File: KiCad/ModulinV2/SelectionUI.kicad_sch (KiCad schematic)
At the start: 24 parts, among them IC16 E-ULN2003D1013TR, IC17 E-ULN2003D1013TR, IC18 CD4028BM96, IC19 CD4028BM96

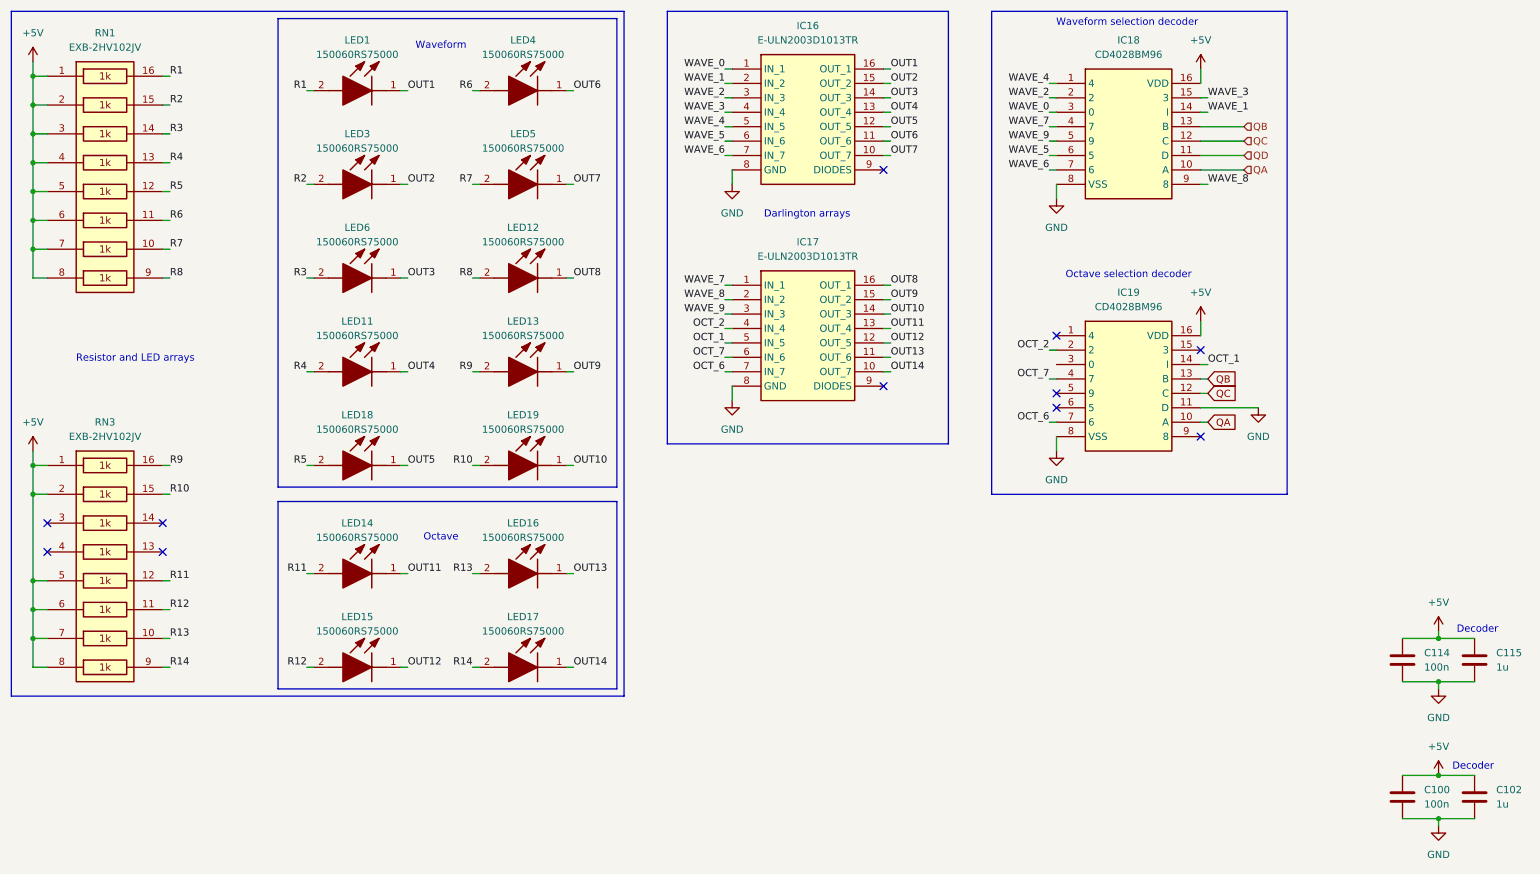
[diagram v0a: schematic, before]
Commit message: Changed switch for the boot and nrst. Fixed the GATE interface trigger
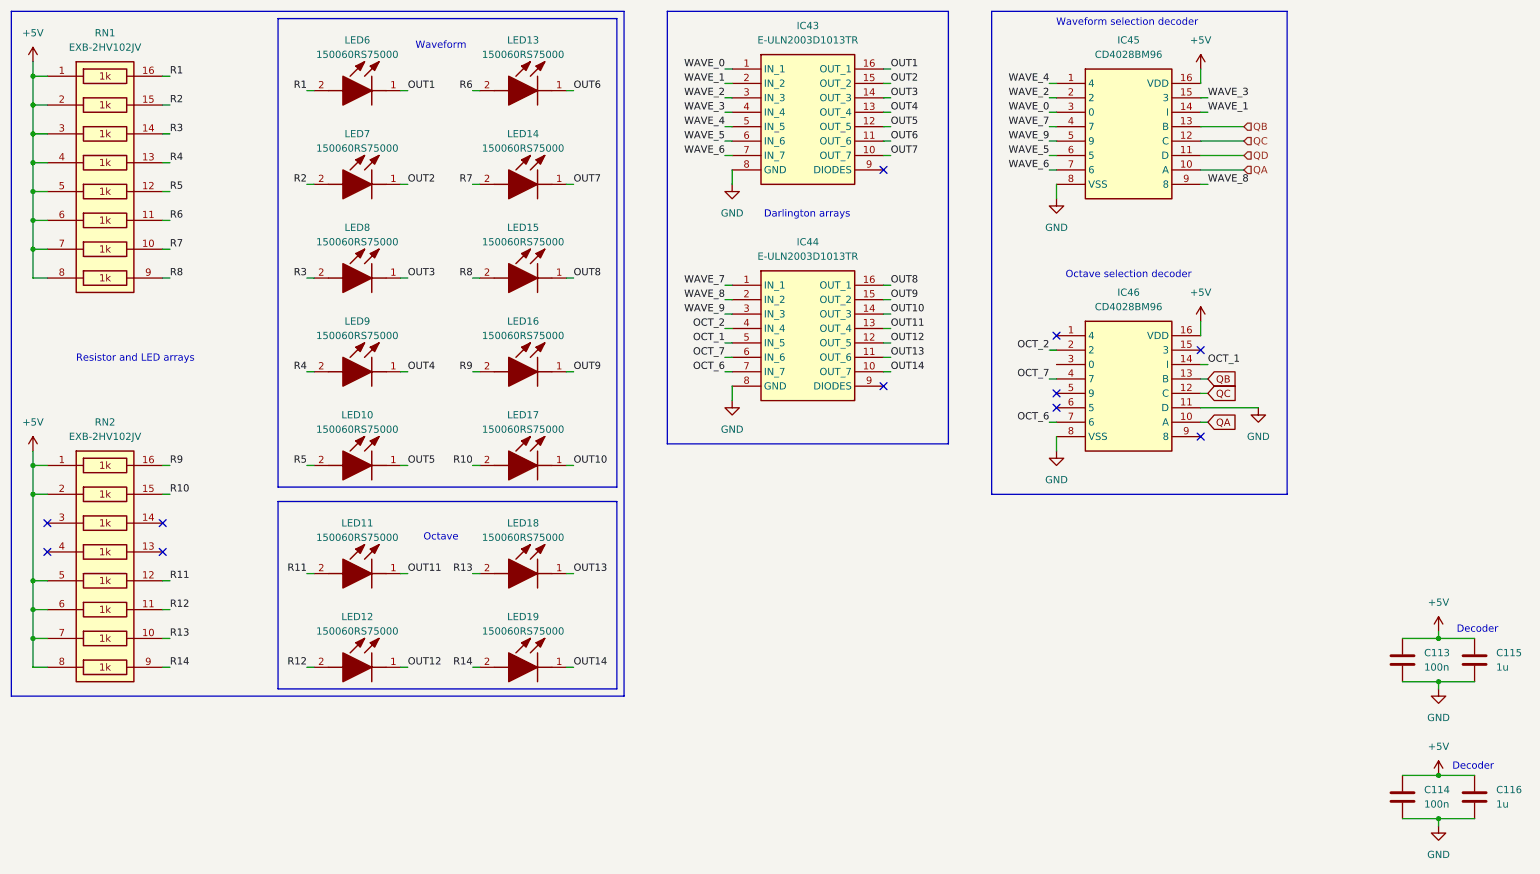
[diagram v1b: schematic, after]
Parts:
- renumbered C114 to C113, C100 to C114, C102 to C116, IC16 to IC43, IC17 to IC44, IC18 to IC45, IC19 to IC46, LED18 to LED10, LED14 to LED11, LED15 to LED12, LED4 to LED13, LED5 to LED14, LED12 to LED15, LED13 to LED16, LED19 to LED17, LED16 to LED18, LED17 to LED19, LED1 to LED6, LED3 to LED7, LED6 to LED8, LED11 to LED9, RN3 to RN2

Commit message: Started adding footprints for capacitors
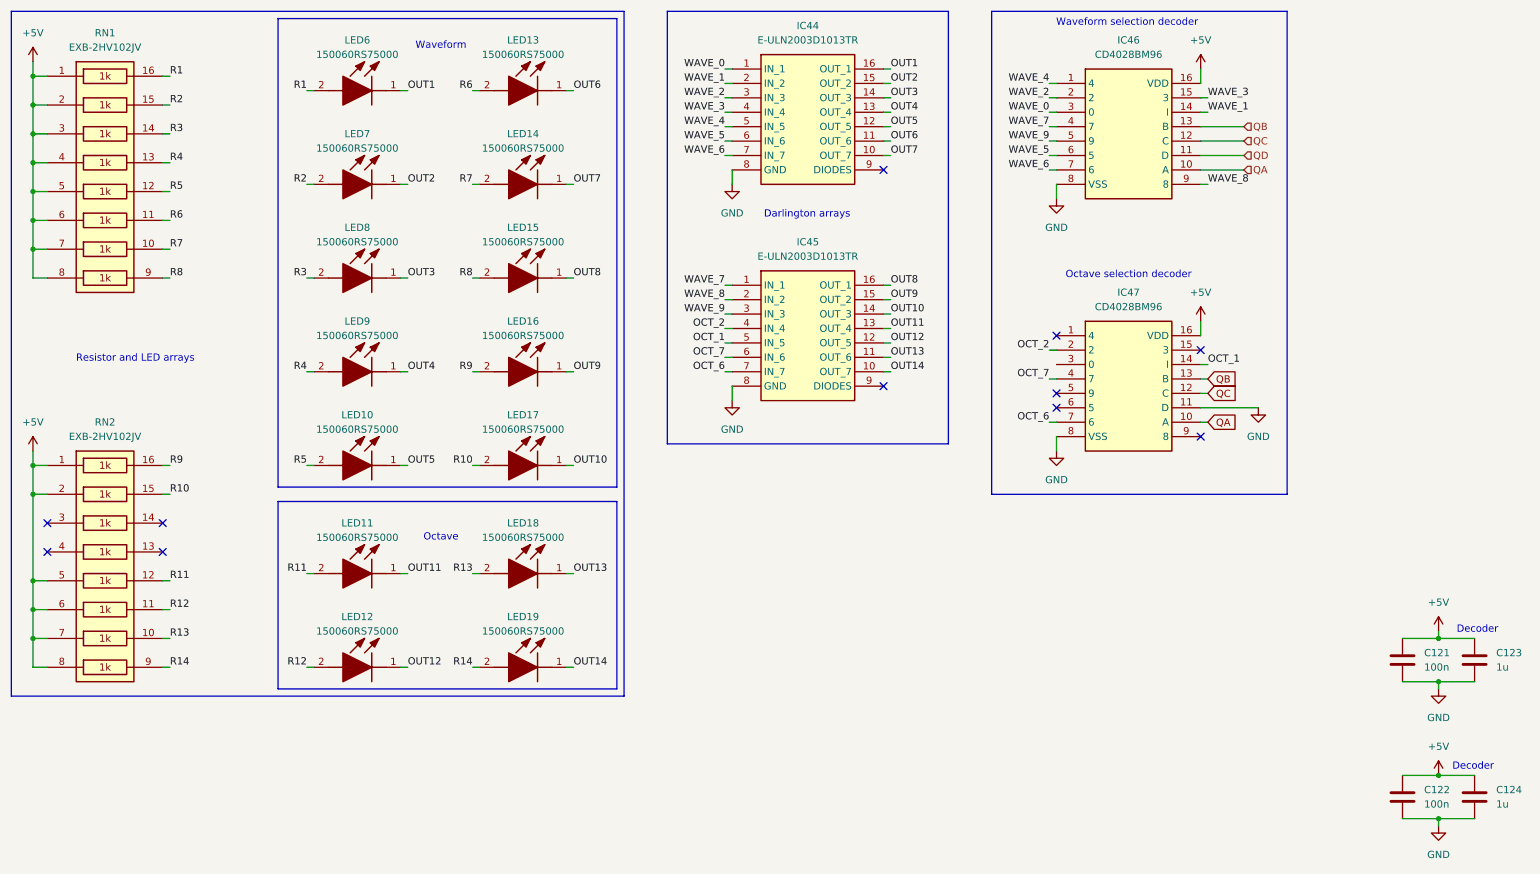
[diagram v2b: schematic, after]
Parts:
- C121: renamed from C113; footprint (none) -> SamacSys_Parts:CAPC1608X90N
- C122: renamed from C114; footprint (none) -> SamacSys_Parts:CAPC1608X90N
- C123: renamed from C115; footprint (none) -> SamacSys_Parts:CAPC1608X95N
- C124: renamed from C116; footprint (none) -> SamacSys_Parts:CAPC1608X95N
- renumbered IC43 to IC44, IC44 to IC45, IC45 to IC46, IC46 to IC47
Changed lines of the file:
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@@
 		(dnp no)
 		(fields_autoplaced yes)
-		(property "Reference" "#PWR0291"
+		(property "Reference" "#PWR0299"
 			(at 265.43 163.83 0)
 			(effects
@@
 			(project "ModulinV2"
 				(path "/c6b34a57-3941-4b56-8b80-1848c7f41082/ba5ade70-a939-4914-9429-1ad400c74d73/e799dfb0-018d-4a0c-90e3-bc5a892eb818"
-					(reference "#PWR0291")
+					(reference "#PWR0299")
 					(unit 1)
 				)
@@
 		(dnp no)
 		(fields_autoplaced yes)
-		(property "Reference" "#PWR0282"
+		(property "Reference" "#PWR0290"
 			(at 140.97 88.9 0)
 			(effects
@@
 			(project "ModulinV2"
 				(path "/c6b34a57-3941-4b56-8b80-1848c7f41082/ba5ade70-a939-4914-9429-1ad400c74d73/e799dfb0-018d-4a0c-90e3-bc5a892eb818"
-					(reference "#PWR0282")
+					(reference "#PWR0290")
 					(unit 1)
 				)
@@
 		(dnp no)
 		(fields_autoplaced yes)
-		(property "Reference" "#PWR0284"
+		(property "Reference" "#PWR0292"
 			(at 198.12 97.79 0)
 			(effects
@@
 			(project "ModulinV2"
 				(path "/c6b34a57-3941-4b56-8b80-1848c7f41082/ba5ade70-a939-4914-9429-1ad400c74d73/e799dfb0-018d-4a0c-90e3-bc5a892eb818"
-					(reference "#PWR0284")
+					(reference "#PWR0292")
 					(unit 1)
 				)
@@
 		(dnp no)
 		(fields_autoplaced yes)
-		(property "Reference" "#PWR0281"
+		(property "Reference" "#PWR0289"
 			(at 140.97 50.8 0)
 			(effects
@@
 			(project ""
 				(path "/c6b34a57-3941-4b56-8b80-1848c7f41082/ba5ade70-a939-4914-9429-1ad400c74d73/e799dfb0-018d-4a0c-90e3-bc5a892eb818"
-					(reference "#PWR0281")
+					(reference "#PWR0289")
 					(unit 1)
 				)
@@
 		(dnp no)
 		(fields_autoplaced yes)
-		(property "Reference" "IC45"
+		(property "Reference" "IC46"
 			(at 210.82 19.05 0)
 			(effects
@@
 			(project ""
 				(path "/c6b34a57-3941-4b56-8b80-1848c7f41082/ba5ade70-a939-4914-9429-1ad400c74d73/e799dfb0-018d-4a0c-90e3-bc5a892eb818"
-					(reference "IC45")
+					(reference "IC46")
 					(unit 1)
 				)
@@
 		(dnp no)
 		(fields_autoplaced yes)
-		(property "Reference" "#PWR0279"
+		(property "Reference" "#PWR0287"
 			(at 17.78 26.67 0)
 			(effects
@@
 			(project ""
 				(path "/c6b34a57-3941-4b56-8b80-1848c7f41082/ba5ade70-a939-4914-9429-1ad400c74d73/e799dfb0-018d-4a0c-90e3-bc5a892eb818"
-					(reference "#PWR0279")
+					(reference "#PWR0287")
 					(unit 1)
 				)
@@
 		(dnp no)
 		(fields_autoplaced yes)
-		(property "Reference" "#PWR0280"
+		(property "Reference" "#PWR0288"
 			(at 17.78 95.25 0)
 			(effects
@@
 			(project "ModulinV2"
 				(path "/c6b34a57-3941-4b56-8b80-1848c7f41082/ba5ade70-a939-4914-9429-1ad400c74d73/e799dfb0-018d-4a0c-90e3-bc5a892eb818"
-					(reference "#PWR0280")
+					(reference "#PWR0288")
 					(unit 1)
 				)
@@
 		(dnp no)
 		(fields_autoplaced yes)
-		(property "Reference" "#PWR0283"
+		(property "Reference" "#PWR0291"
 			(at 198.12 53.34 0)
 			(effects
@@
 			(project "ModulinV2"
 				(path "/c6b34a57-3941-4b56-8b80-1848c7f41082/ba5ade70-a939-4914-9429-1ad400c74d73/e799dfb0-018d-4a0c-90e3-bc5a892eb818"
-					(reference "#PWR0283")
+					(reference "#PWR0291")
 					(unit 1)
 				)
@@
 		(dnp no)
 		(fields_autoplaced yes)
-		(property "Reference" "IC43"
+		(property "Reference" "IC44"
 			(at 154.305 16.51 0)
 			(effects
@@
 			(project ""
 				(path "/c6b34a57-3941-4b56-8b80-1848c7f41082/ba5ade70-a939-4914-9429-1ad400c74d73/e799dfb0-018d-4a0c-90e3-bc5a892eb818"
-					(reference "IC43")
+					(reference "IC44")
 					(unit 1)
 				)
@@
 		(dnp no)
 		(fields_autoplaced yes)
-		(property "Reference" "IC44"
+		(property "Reference" "IC45"
 			(at 154.305 54.61 0)
 			(effects
@@
 			(project "ModulinV2"
 				(path "/c6b34a57-3941-4b56-8b80-1848c7f41082/ba5ade70-a939-4914-9429-1ad400c74d73/e799dfb0-018d-4a0c-90e3-bc5a892eb818"
-					(reference "IC44")
+					(reference "IC45")
 					(unit 1)
 				)
@@
 		(dnp no)
 		(fields_autoplaced yes)
-		(property "Reference" "C113"
+		(property "Reference" "C121"
 			(at 262.89 126.9999 0)
 			(effects
@@
 			)
 		)
-		(property "Footprint" ""
+		(property "Footprint" "SamacSys_Parts:CAPC1608X90N"
 			(at 258.1148 124.46 0)
 			(effects
@@
 			(project "ModulinV2"
 				(path "/c6b34a57-3941-4b56-8b80-1848c7f41082/ba5ade70-a939-4914-9429-1ad400c74d73/e799dfb0-018d-4a0c-90e3-bc5a892eb818"
-					(reference "C113")
+					(reference "C121")
 					(unit 1)
 				)
@@
 		(dnp no)
 		(fields_autoplaced yes)
-		(property "Reference" "#PWR0288"
+		(property "Reference" "#PWR0296"
 			(at 265.43 127 0)
 			(effects
@@
 			(project "ModulinV2"
 				(path "/c6b34a57-3941-4b56-8b80-1848c7f41082/ba5ade70-a939-4914-9429-1ad400c74d73/e799dfb0-018d-4a0c-90e3-bc5a892eb818"
-					(reference "#PWR0288")
+					(reference "#PWR0296")
 					(unit 1)
 				)
@@
 		(dnp no)
 		(fields_autoplaced yes)
-		(property "Reference" "C115"
+		(property "Reference" "C123"
 			(at 275.59 126.9999 0)
 			(effects
@@
 			)
 		)
-		(property "Footprint" ""
+		(property "Footprint" "SamacSys_Parts:CAPC1608X95N"
 			(at 270.8148 124.46 0)
 			(effects
@@
 			(project "ModulinV2"
 				(path "/c6b34a57-3941-4b56-8b80-1848c7f41082/ba5ade70-a939-4914-9429-1ad400c74d73/e799dfb0-018d-4a0c-90e3-bc5a892eb818"
-					(reference "C115")
+					(reference "C123")
 					(unit 1)
 				)
@@
 		(dnp no)
 		(fields_autoplaced yes)
-		(property "Reference" "#PWR0286"
+		(property "Reference" "#PWR0294"
 			(at 223.52 72.39 0)
 			(effects
@@
 			(project "ModulinV2"
 				(path "/c6b34a57-3941-4b56-8b80-1848c7f41082/ba5ade70-a939-4914-9429-1ad400c74d73/e799dfb0-018d-4a0c-90e3-bc5a892eb818"
-					(reference "#PWR0286")
+					(reference "#PWR0294")
 					(unit 1)
 				)
@@
 		(dnp no)
 		(fields_autoplaced yes)
-		(property "Reference" "#PWR0285"
+		(property "Reference" "#PWR0293"
 			(at 223.52 27.94 0)
 			(effects
@@
 			(project "ModulinV2"
 				(path "/c6b34a57-3941-4b56-8b80-1848c7f41082/ba5ade70-a939-4914-9429-1ad400c74d73/e799dfb0-018d-4a0c-90e3-bc5a892eb818"
-					(reference "#PWR0285")
+					(reference "#PWR0293")
 					(unit 1)
 				)
@@
 		(dnp no)
 		(fields_autoplaced yes)
-		(property "Reference" "C114"
+		(property "Reference" "C122"
 			(at 262.89 151.1299 0)
 			(effects
@@
 			)
 		)
-		(property "Footprint" ""
+		(property "Footprint" "SamacSys_Parts:CAPC1608X90N"
 			(at 258.1148 148.59 0)
 			(effects
@@
 			(project "ModulinV2"
 				(path "/c6b34a57-3941-4b56-8b80-1848c7f41082/ba5ade70-a939-4914-9429-1ad400c74d73/e799dfb0-018d-4a0c-90e3-bc5a892eb818"
-					(reference "C114")
+					(reference "C122")
 					(unit 1)
 				)
@@
 		(dnp no)
 		(fields_autoplaced yes)
-		(property "Reference" "#PWR0287"
+		(property "Reference" "#PWR0295"
 			(at 233.68 90.17 0)
 			(effects
@@
 			(project "ModulinV2"
 				(path "/c6b34a57-3941-4b56-8b80-1848c7f41082/ba5ade70-a939-4914-9429-1ad400c74d73/e799dfb0-018d-4a0c-90e3-bc5a892eb818"
-					(reference "#PWR0287")
+					(reference "#PWR0295")
 					(unit 1)
 				)
@@
 		(dnp no)
 		(fields_autoplaced yes)
-		(property "Reference" "#PWR0289"
+		(property "Reference" "#PWR0297"
 			(at 265.43 139.7 0)
 			(effects
@@
 			(project "ModulinV2"
 				(path "/c6b34a57-3941-4b56-8b80-1848c7f41082/ba5ade70-a939-4914-9429-1ad400c74d73/e799dfb0-018d-4a0c-90e3-bc5a892eb818"
-					(reference "#PWR0289")
+					(reference "#PWR0297")
 					(unit 1)
 				)
@@
 		(dnp no)
 		(fields_autoplaced yes)
-		(property "Reference" "#PWR0290"
+		(property "Reference" "#PWR0298"
 			(at 265.43 152.4 0)
 			(effects
@@
 			(project "ModulinV2"
 				(path "/c6b34a57-3941-4b56-8b80-1848c7f41082/ba5ade70-a939-4914-9429-1ad400c74d73/e799dfb0-018d-4a0c-90e3-bc5a892eb818"
-					(reference "#PWR0290")
+					(reference "#PWR0298")
 					(unit 1)
 				)
@@
 		(dnp no)
 		(fields_autoplaced yes)
-		(property "Reference" "IC46"
+		(property "Reference" "IC47"
 			(at 210.82 63.5 0)
 			(effects
@@
 			(project "ModulinV2"
 				(path "/c6b34a57-3941-4b56-8b80-1848c7f41082/ba5ade70-a939-4914-9429-1ad400c74d73/e799dfb0-018d-4a0c-90e3-bc5a892eb818"
-					(reference "IC46")
+					(reference "IC47")
 					(unit 1)
 				)
@@
 		(dnp no)
 		(fields_autoplaced yes)
-		(property "Reference" "C116"
+		(property "Reference" "C124"
 			(at 275.59 151.1299 0)
 			(effects
@@
 			)
 		)
-		(property "Footprint" ""
+		(property "Footprint" "SamacSys_Parts:CAPC1608X95N"
 			(at 270.8148 148.59 0)
 			(effects
@@
 			(project "ModulinV2"
 				(path "/c6b34a57-3941-4b56-8b80-1848c7f41082/ba5ade70-a939-4914-9429-1ad400c74d73/e799dfb0-018d-4a0c-90e3-bc5a892eb818"
-					(reference "C116")
+					(reference "C124")
 					(unit 1)
 				)
